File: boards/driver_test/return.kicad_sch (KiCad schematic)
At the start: 8 parts

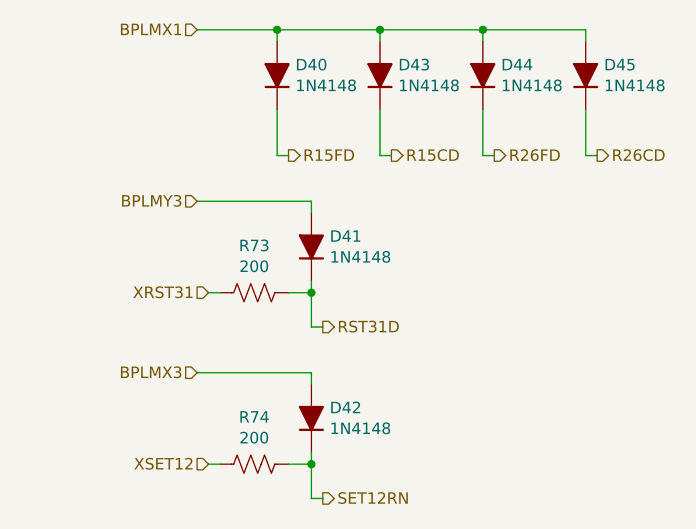
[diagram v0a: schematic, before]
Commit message: Driver: some high-level board rearrangement and addition of 3d models
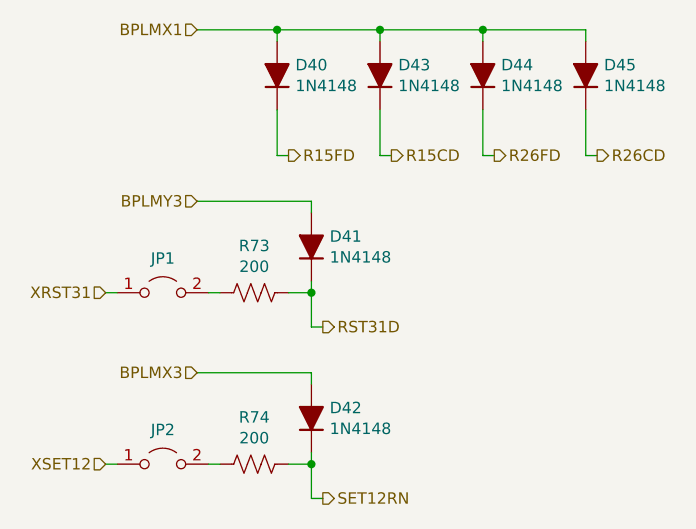
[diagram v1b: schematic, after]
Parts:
- added JP1, JP2: Jumper_2_Open, Connector_PinHeader_2.00mm:PinHeader_1x02_P2.00mm_Vertical, symbol Jumper:Jumper_2_Open
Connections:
- net XRST31: now also JP1.1 (A); no longer R73.1
- net XSET12: now also JP2.1 (A); no longer R74.1
- new net: JP1.2 (B), R73.1
- new net: JP2.2 (B), R74.1
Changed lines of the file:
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@@
+    (stroke (width 0) (type default) (color 0 0 0 0))
+  )
+  (wire (pts (xy 105.41 123.19) (xy 106.68 123.19))
     (stroke (width 0) (type default) (color 0 0 0 0))
   )
@@
     (stroke (width 0) (type default) (color 0 0 0 0))
   )
+  (wire (pts (xy 105.41 104.14) (xy 106.68 104.14))
+    (stroke (width 0) (type default) (color 0 0 0 0))
+  )
   (wire (pts (xy 115.57 113.03) (xy 128.27 113.03))
     (stroke (width 0) (type default) (color 0 0 0 0))
@@
     (effects (font (size 1.27 1.27)) (justify right))
   )
-  (hierarchical_label "XSET12" (shape input) (at 116.84 123.19 180)
+  (hierarchical_label "XSET12" (shape input) (at 105.41 123.19 180)
     (effects (font (size 1.27 1.27)) (justify right))
   )
@@
     (effects (font (size 1.27 1.27)) (justify left))
   )
-  (hierarchical_label "XRST31" (shape input) (at 116.84 104.14 180)
+  (hierarchical_label "XRST31" (shape input) (at 105.41 104.14 180)
     (effects (font (size 1.27 1.27)) (justify right))
   )
@@
       (effects (font (size 1.27 1.27)) hide)
     )
+    (pin "1")
+    (pin "2")
+  )
+  (symbol (lib_id "Jumper:Jumper_2_Open") (at 111.76 123.19 0) (unit 1)
+    (in_bom yes) (on_board yes) (fields_autoplaced)
+    (property "Reference" "JP2" (id 0) (at 111.76 119.38 0))
+    (property "Value" "Jumper_2_Open" (id 1) (at 111.76 119.38 0)
+      (effects (font (size 1.27 1.27)) hide)
+    )
+    (property "Footprint" "Connector_PinHeader_2.00mm:PinHeader_1x02_P2.00mm_Vertical" (id 2) (at 111.76 123.19 0)
+      (effects (font (size 1.27 1.27)) hide)
+    )
+    (property "Datasheet" "~" (id 3) (at 111.76 123.19 0)
+      (effects (font (size 1.27 1.27)) hide)
+    )
+    (pin "1")
+    (pin "2")
+  )
+  (symbol (lib_id "Jumper:Jumper_2_Open") (at 111.76 104.14 0) (unit 1)
+    (in_bom yes) (on_board yes) (fields_autoplaced)
+    (property "Reference" "JP1" (id 0) (at 111.76 100.33 0))
+    (property "Value" "Jumper_2_Open" (id 1) (at 111.76 100.33 0)
+      (effects (font (size 1.27 1.27)) hide)
+    )
+    (property "Footprint" "Connector_PinHeader_2.00mm:PinHeader_1x02_P2.00mm_Vertical" (id 2) (at 111.76 104.14 0)
+      (effects (font (size 1.27 1.27)) hide)
+    )
+    (property "Datasheet" "~" (id 3) (at 111.76 104.14 0)
+      (effects (font (size 1.27 1.27)) hide)
+    )

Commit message: Driver test: finished up board layout
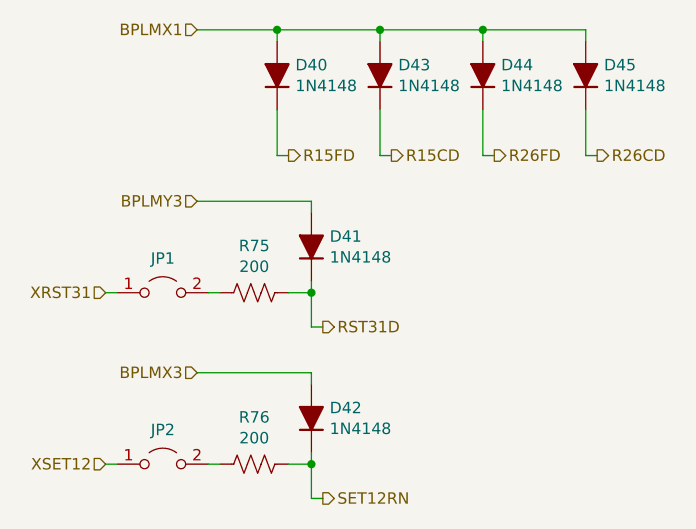
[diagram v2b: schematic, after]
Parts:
- renumbered R73 to R75, R74 to R76
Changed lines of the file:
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@@
   (symbol (lib_id "Device:R_US") (at 121.92 104.14 90) (unit 1)
     (in_bom yes) (on_board yes)
-    (property "Reference" "R73" (id 0) (at 121.92 98.933 90))
+    (property "Reference" "R75" (id 0) (at 121.92 98.933 90))
     (property "Value" "200" (id 1) (at 121.92 101.2444 90))
     (property "Footprint" "Resistor_SMD:R_0603_1608Metric" (id 2) (at 122.174 103.124 90)
@@
   (symbol (lib_id "Device:R_US") (at 121.92 123.19 90) (unit 1)
     (in_bom yes) (on_board yes)
-    (property "Reference" "R74" (id 0) (at 121.92 117.983 90))
+    (property "Reference" "R76" (id 0) (at 121.92 117.983 90))
     (property "Value" "200" (id 1) (at 121.92 120.2944 90))
     (property "Footprint" "Resistor_SMD:R_0603_1608Metric" (id 2) (at 122.174 122.174 90)
